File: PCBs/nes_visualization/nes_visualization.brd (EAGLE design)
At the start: 99.8 x 31.8 mm, 12 parts, among them U1 TLC59282

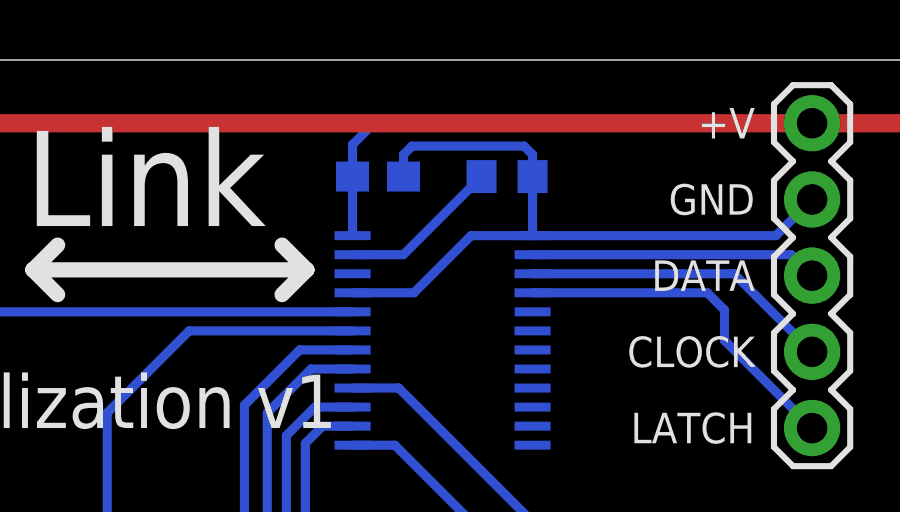
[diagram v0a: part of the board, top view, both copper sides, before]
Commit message: NES Visualization: Changed the reference resistor to 0805 size.
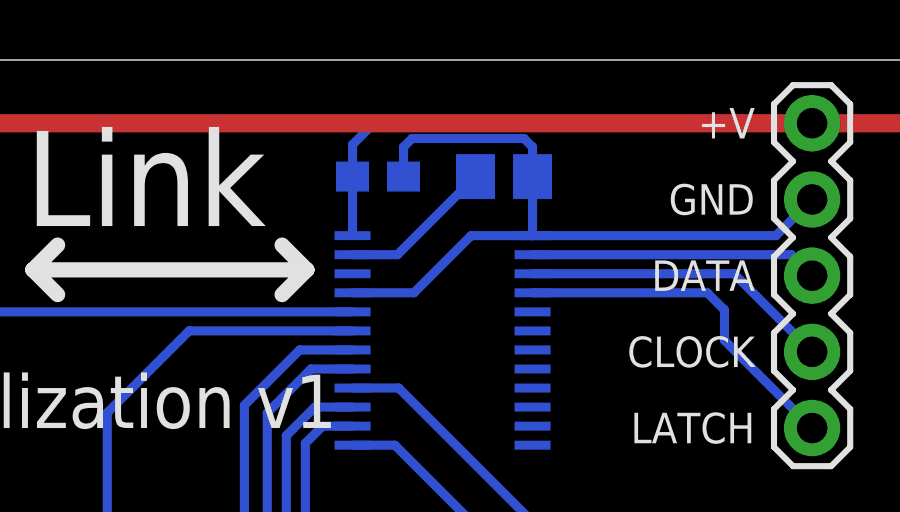
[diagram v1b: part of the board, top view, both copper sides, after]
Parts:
- R13: device rcl:R0603 -> rcl:R0805
- moved R13 0.10 mm to (34.7, 27.9)
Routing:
- net GND: track 24.6 -> 25.1 mm
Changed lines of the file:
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@@
 <layer number="20" name="Dimension" color="15" fill="1" visible="yes" active="yes"/>
 <layer number="21" name="tPlace" color="7" fill="1" visible="yes" active="yes"/>
-<layer number="22" name="bPlace" color="7" fill="1" visible="no" active="yes"/>
+<layer number="22" name="bPlace" color="7" fill="1" visible="yes" active="yes"/>
 <layer number="23" name="tOrigins" color="15" fill="1" visible="yes" active="yes"/>
 <layer number="24" name="bOrigins" color="15" fill="1" visible="yes" active="yes"/>
@@
 <layer number="28" name="bValues" color="7" fill="1" visible="yes" active="yes"/>
 <layer number="29" name="tStop" color="7" fill="3" visible="yes" active="yes"/>
-<layer number="30" name="bStop" color="7" fill="6" visible="no" active="yes"/>
+<layer number="30" name="bStop" color="7" fill="6" visible="yes" active="yes"/>
 <layer number="31" name="tCream" color="7" fill="4" visible="yes" active="yes"/>
-<layer number="32" name="bCream" color="7" fill="5" visible="no" active="yes"/>
+<layer number="32" name="bCream" color="7" fill="5" visible="yes" active="yes"/>
 <layer number="33" name="tFinish" color="6" fill="3" visible="yes" active="yes"/>
-<layer number="34" name="bFinish" color="6" fill="6" visible="no" active="yes"/>
+<layer number="34" name="bFinish" color="6" fill="6" visible="yes" active="yes"/>
 <layer number="35" name="tGlue" color="7" fill="4" visible="yes" active="yes"/>
-<layer number="36" name="bGlue" color="7" fill="5" visible="no" active="yes"/>
+<layer number="36" name="bGlue" color="7" fill="5" visible="yes" active="yes"/>
 <layer number="37" name="tTest" color="7" fill="1" visible="yes" active="yes"/>
 <layer number="38" name="bTest" color="7" fill="1" visible="yes" active="yes"/>
@@
 <layer number="47" name="Measures" color="7" fill="1" visible="yes" active="yes"/>
 <layer number="48" name="Document" color="7" fill="1" visible="yes" active="yes"/>
-<layer number="49" name="Reference" color="7" fill="1" visible="no" active="yes"/>
+<layer number="49" name="Reference" color="7" fill="1" visible="yes" active="yes"/>
 <layer number="50" name="dxf" color="7" fill="1" visible="no" active="no"/>
 <layer number="51" name="tDocu" color="7" fill="1" visible="yes" active="yes"/>
@@
 <attribute name="MOUSER#" value="80-C0603C104K5R" x="64.779" y="64.77" size="1.778" layer="28" rot="MR180" display="off"/>
 </element>
-<element name="R13" library="rcl" package="R0603" value="25k" x="34.789" y="27.94" smashed="yes" rot="MR0"/>
+<element name="R13" library="rcl" package="R0805" value="25k" x="34.689" y="27.94" smashed="yes" rot="MR0"/>
 <element name="LED1" library="led" package="LED5MM" value="" x="4.4196" y="8.5344" smashed="yes" rot="MR0">
 <attribute name="VALUE" x="1.2192" y="6.731" size="1.27" layer="28" ratio="10" rot="MR0"/>
@@
 <wire x1="33.5915" y1="25.9715" x2="35.639" y2="25.9715" width="0.3048" layer="16"/>
 <wire x1="35.639" y1="27.94" x2="35.639" y2="25.9715" width="0.3048" layer="16"/>
-<wire x1="31.339" y1="27.94" x2="31.339" y2="28.672" width="0.3048" layer="16"/>
-<wire x1="31.339" y1="28.672" x2="31.623" y2="28.956" width="0.3048" layer="16"/>
-<wire x1="35.639" y1="27.94" x2="35.639" y2="28.672" width="0.3048" layer="16"/>
-<wire x1="31.623" y1="28.956" x2="35.355" y2="28.956" width="0.3048" layer="16"/>
-<wire x1="35.355" y1="28.956" x2="35.639" y2="28.672" width="0.3048" layer="16"/>
+<wire x1="31.339" y1="27.94" x2="31.339" y2="28.926" width="0.3048" layer="16"/>
+<wire x1="31.339" y1="28.926" x2="31.623" y2="29.21" width="0.3048" layer="16"/>
+<wire x1="35.639" y1="27.94" x2="35.639" y2="28.926" width="0.3048" layer="16"/>
+<wire x1="31.623" y1="29.21" x2="35.355" y2="29.21" width="0.3048" layer="16"/>
+<wire x1="35.355" y1="29.21" x2="35.639" y2="28.926" width="0.3048" layer="16"/>
 </signal>
 <signal name="N$5">
 <contactref element="R13" pad="2"/>
 <contactref element="U1" pad="23"/>
-<wire x1="29.639" y1="25.3365" x2="31.3355" y2="25.3365" width="0.3048" layer="16"/>
-<wire x1="31.3355" y1="25.3365" x2="33.939" y2="27.94" width="0.3048" layer="16"/>
+<wire x1="29.639" y1="25.3365" x2="31.1355" y2="25.3365" width="0.3048" layer="16"/>
+<wire x1="31.1355" y1="25.3365" x2="33.739" y2="27.94" width="0.3048" layer="16"/>
 </signal>
 <signal name="A_LED">
